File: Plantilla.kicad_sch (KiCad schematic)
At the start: 12 parts, among them J1 Screw_Terminal_01x03, Q1 IRF540N, U1 TIMER 555

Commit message: khv
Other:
- note added: "DIMMER 555"
- note removed: "DIMMER 5"
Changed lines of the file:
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@@
 		(company "UPNA")
 	)
-	(text "DIMMER 5"
+	(text "DIMMER 555"
 		(exclude_from_sim no)
 		(at 151.13 45.212 0)
@@
 			(justify left bottom)
 		)
-		(property "Clase de red" "GND"
+		(property "Netclass" "GND"
 			(at 168.3385 140.97 0)
 			(show_name no)
@@
 			(justify left bottom)
 		)
-		(property "Clase de red" "VCC"
+		(property "Netclass" "VCC"
 			(at 141.6685 91.44 0)
 			(show_name no)
@@
 			(justify right bottom)
 		)
-		(property "Clase de red" "SIGNAL"
+		(property "Netclass" "SIGNAL"
 			(at 181.0385 128.27 0)
 			(show_name no)

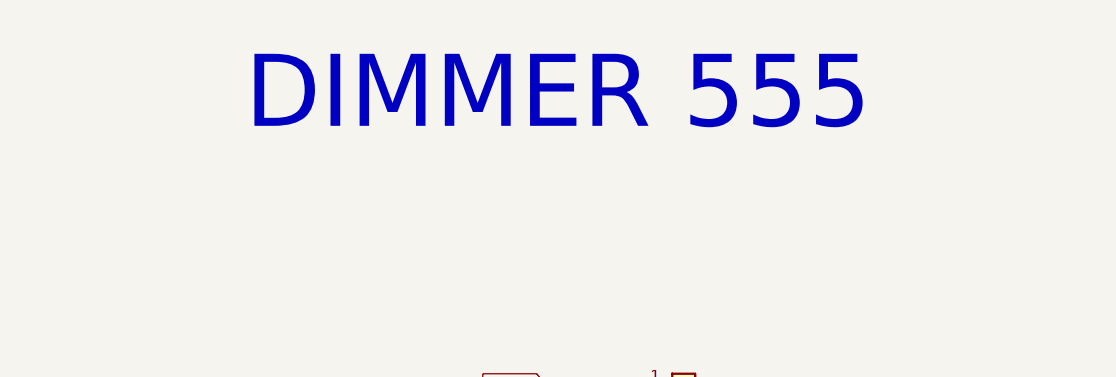
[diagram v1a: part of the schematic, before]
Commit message: Revert "Merge branch 'main' of https://github.com/boquepasa/Plantilla"
This reverts commit d51ca88810657ef9873862f617c491b9a8def481, reversing
changes made to 5b42f346ed9f3a54989fdb3635692f82da783504.
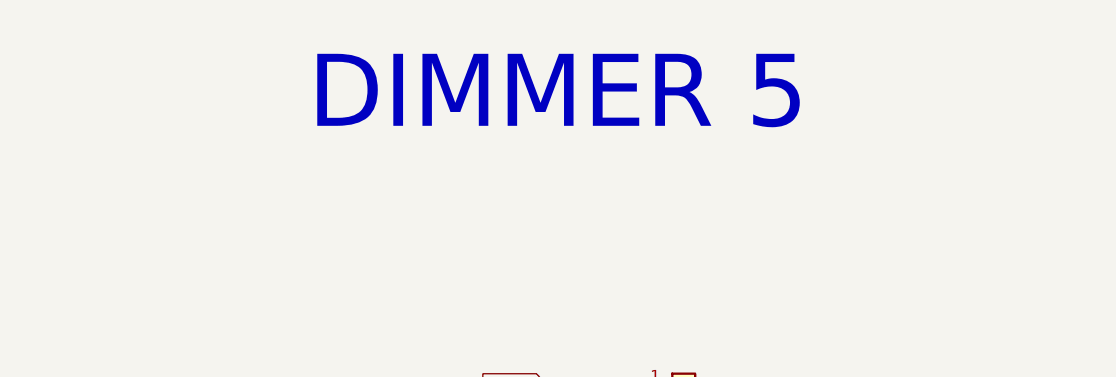
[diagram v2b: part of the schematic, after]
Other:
- note added: "DIMMER 5"
- note removed: "DIMMER 555"
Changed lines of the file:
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@@
 		(company "UPNA")
 	)
-	(text "DIMMER 555"
+	(text "DIMMER 5"
 		(exclude_from_sim no)
 		(at 151.13 45.212 0)
@@
 			(justify left bottom)
 		)
-		(property "Netclass" "GND"
+		(property "Clase de red" "GND"
 			(at 168.3385 140.97 0)
 			(show_name no)
@@
 			(justify left bottom)
 		)
-		(property "Netclass" "VCC"
+		(property "Clase de red" "VCC"
 			(at 141.6685 91.44 0)
 			(show_name no)
@@
 			(justify right bottom)
 		)
-		(property "Netclass" "SIGNAL"
+		(property "Clase de red" "SIGNAL"
 			(at 181.0385 128.27 0)
 			(show_name no)

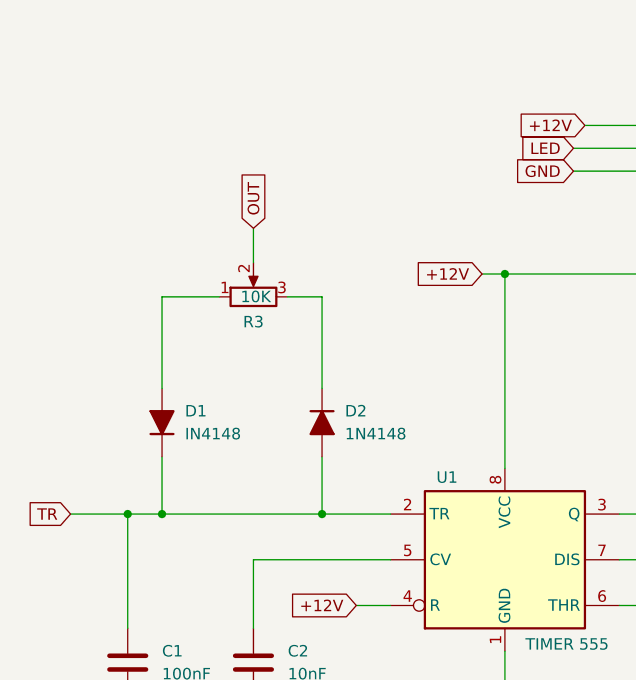
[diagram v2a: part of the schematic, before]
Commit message: Organizaci�n de las conexiones del potenci�metro en el esquem�tico.
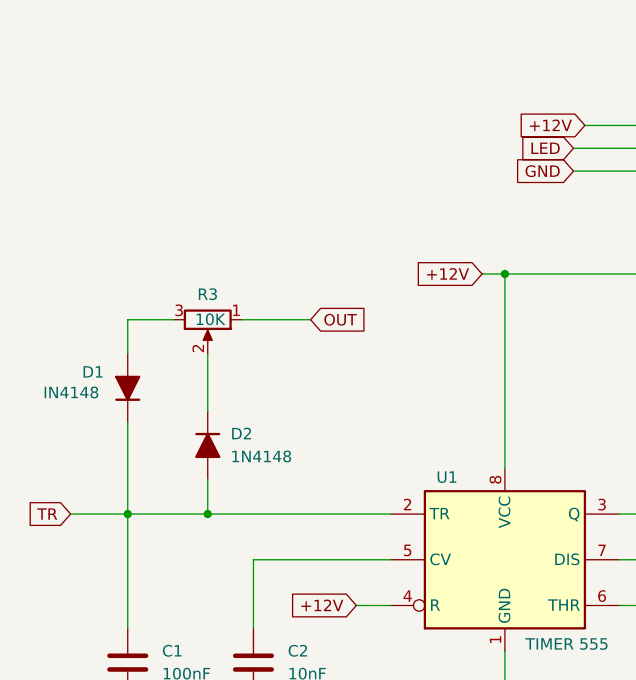
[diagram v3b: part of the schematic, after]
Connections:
- net OUT: now also R3.1; no longer R3.2
- net at D1.2 (A): now also R3.3; no longer R3.1
- net at D2.1 (K): now also R3.2; no longer R3.3
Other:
- moved on the sheet: D1, D2, R3
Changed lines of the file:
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@@
-	)
-	(junction
-		(at 120.65 120.65)
-		(diameter 0)
-		(color 0 0 0 0)
 	)
 	(junction
@@
 	)
 	(junction
-		(at 102.87 120.65)
+		(at 107.95 120.65)
 		(diameter 0)
 		(color 0 0 0 0)
@@
 	(wire
 		(pts
-			(xy 102.87 120.65) (xy 99.06 120.65)
-		)
-		(stroke
-			(width 0)
-			(type default)
-		)
-	)
-	(wire
-		(pts
 			(xy 148.59 82.55) (xy 160.02 82.55)
 		)
@@
 	(wire
 		(pts
+			(xy 99.06 120.65) (xy 128.27 120.65)
+		)
+		(stroke
+			(width 0)
+			(type default)
+		)
+	)
+	(wire
+		(pts
+			(xy 111.76 99.06) (xy 119.38 99.06)
+		)
+		(stroke
+			(width 0)
+			(type default)
+		)
+	)
+	(wire
+		(pts
 			(xy 201.93 118.11) (xy 219.71 118.11)
 		)
@@
 	(wire
 		(pts
-			(xy 120.65 120.65) (xy 120.65 114.3)
+			(xy 99.06 99.06) (xy 104.14 99.06)
+		)
+		(stroke
+			(width 0)
+			(type default)
+		)
+	)
+	(wire
+		(pts
+			(xy 107.95 120.65) (xy 107.95 116.84)
 		)
 		(stroke
@@
 	(wire
 		(pts
-			(xy 120.65 120.65) (xy 102.87 120.65)
-		)
-		(stroke
-			(width 0)
-			(type default)
-		)
-	)
-	(wire
-		(pts
 			(xy 99.06 120.65) (xy 99.06 133.35)
 		)
@@
 	(wire
 		(pts
-			(xy 116.84 96.52) (xy 120.65 96.52)
-		)
-		(stroke
-			(width 0)
-			(type default)
-		)
-	)
-	(wire
-		(pts
 			(xy 149.86 77.47) (xy 160.02 77.47)
 		)
@@
 	(wire
 		(pts
-			(xy 120.65 96.52) (xy 120.65 106.68)
+			(xy 107.95 102.87) (xy 107.95 109.22)
 		)
 		(stroke
@@
 	(wire
 		(pts
-			(xy 102.87 114.3) (xy 102.87 120.65)
-		)
-		(stroke
-			(width 0)
-			(type default)
-		)
-	)
-	(wire
-		(pts
-			(xy 113.03 88.9) (xy 113.03 92.71)
+			(xy 99.06 110.49) (xy 99.06 120.65)
 		)
 		(stroke
@@
 	(wire
 		(pts
-			(xy 102.87 96.52) (xy 102.87 106.68)
-		)
-		(stroke
-			(width 0)
-			(type default)
-		)
-	)
-	(wire
-		(pts
-			(xy 128.27 120.65) (xy 120.65 120.65)
+			(xy 99.06 99.06) (xy 99.06 102.87)
 		)
 		(stroke
@@
 		(pts
 			(xy 113.03 143.51) (xy 113.03 140.97)
-		)
-		(stroke
-			(width 0)
-			(type default)
-		)
-	)
-	(wire
-		(pts
-			(xy 109.22 96.52) (xy 102.87 96.52)
 		)
 		(stroke
@@
 	(global_label "OUT"
 		(shape input)
-		(at 113.03 88.9 90)
+		(at 119.38 99.06 0)
 		(fields_autoplaced yes)
 		(effects
@@
 		)
 		(property "Intersheetrefs" "${INTERSHEET_REFS}"
-			(at 113.03 82.2862 90)
+			(at 125.9938 99.06 0)
 			(hide yes)
 			(show_name no)
@@
 	(symbol
 		(lib_id "Device:R_Potentiometer")
-		(at 113.03 96.52 90)
+		(at 107.95 99.06 270)
 		(unit 1)
 		(body_style 1)
@@
 		(dnp no)
 		(property "Reference" "R3"
-			(at 113.03 99.314 90)
+			(at 107.95 96.266 90)
 			(show_name no)
 			(do_not_autoplace no)
@@
 		)
 		(property "Value" "10K"
-			(at 113.284 96.52 90)
+			(at 108.204 99.06 90)
 			(show_name no)
 			(do_not_autoplace no)
@@
 		)
 		(property "Footprint" "Potentiometer_SMD:Potentiometer_Bourns_3314G_Vertical"
-			(at 113.03 96.52 0)
+			(at 107.95 99.06 0)
 			(hide yes)
 			(show_name no)
@@
 		)
 		(property "Datasheet" ""
-			(at 113.03 96.52 0)
+			(at 107.95 99.06 0)
 			(hide yes)
 			(show_name no)
@@
 		)
 		(property "Description" "Potentiometer"
-			(at 113.03 96.52 0)
+			(at 107.95 99.06 0)
 			(hide yes)
 			(show_name no)
@@
 	(symbol
 		(lib_id "Device:D_Filled")
-		(at 102.87 110.49 90)
+		(at 99.06 106.68 90)
 		(unit 1)
 		(body_style 1)
@@
 		(in_pos_files yes)
 		(dnp no)
-		(fields_autoplaced yes)
 		(property "Reference" "D1"
-			(at 105.41 109.2199 90)
+			(at 93.98 104.902 90)
 			(show_name no)
 			(do_not_autoplace no)
@@
 		)
 		(property "Value" "IN4148"
-			(at 105.41 111.7599 90)
+			(at 89.662 107.188 90)
 			(show_name no)
 			(do_not_autoplace no)
@@
 		)
 		(property "Footprint" "Diode_SMD:D_SOD-128"
-			(at 102.87 110.49 0)
+			(at 99.06 106.68 0)
 			(hide yes)
 			(show_name no)
@@
 		)
 		(property "Datasheet" ""
-			(at 102.87 110.49 0)
+			(at 99.06 106.68 0)
 			(hide yes)
 			(show_name no)
@@
 		)
 		(property "Description" "Diode, filled shape"
-			(at 102.87 110.49 0)
+			(at 99.06 106.68 0)
 			(hide yes)
 			(show_name no)
@@
 		)
 		(property "Sim.Device" "D"
-			(at 102.87 110.49 0)
+			(at 99.06 106.68 0)
 			(hide yes)
 			(show_name no)
@@
 		)
 		(property "Sim.Pins" "1=K 2=A"
-			(at 102.87 110.49 0)
+			(at 99.06 106.68 0)
 			(hide yes)
 			(show_name no)
@@
 	(symbol
 		(lib_id "Device:D_Filled")
-		(at 120.65 110.49 270)
+		(at 107.95 113.03 270)
 		(unit 1)
 		(body_style 1)
@@
 		(fields_autoplaced yes)
 		(property "Reference" "D2"
-			(at 123.19 109.2199 90)
+			(at 110.49 111.7599 90)
 			(show_name no)
 			(do_not_autoplace no)
@@
 		)
 		(property "Value" "1N4148"
-			(at 123.19 111.7599 90)
+			(at 110.49 114.2999 90)
 			(show_name no)
 			(do_not_autoplace no)
@@
 		)
 		(property "Footprint" "Diode_SMD:D_SOD-128"
-			(at 120.65 110.49 0)
+			(at 107.95 113.03 0)
 			(hide yes)
 			(show_name no)
@@
 		)
 		(property "Datasheet" ""
-			(at 120.65 110.49 0)
+			(at 107.95 113.03 0)
 			(hide yes)
 			(show_name no)
@@
 		)
 		(property "Description" "Diode, filled shape"
-			(at 120.65 110.49 0)
+			(at 107.95 113.03 0)
 			(hide yes)
 			(show_name no)
@@
 		)
 		(property "Sim.Device" "D"
-			(at 120.65 110.49 0)
+			(at 107.95 113.03 0)
 			(hide yes)
 			(show_name no)
@@
 		)
 		(property "Sim.Pins" "1=K 2=A"
-			(at 120.65 110.49 0)
-			(hide yes)
-			(show_name no)
+			(at 107.95 113.03 0)
+			(hide yes)
+			(show_name no)
